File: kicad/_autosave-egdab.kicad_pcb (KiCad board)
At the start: 4 copper layers, 93.4 x 99.4 mm, 56 parts, among them J2 Conn_02x03_Counter_Clockwise, J3 Conn_02x04_Counter_Clockwise, SW1 SW_DIP_x04, SW2 SW_Push, SW6 SW_SPST, U1 ATtiny1606-S, U2 AS1115-BSST, U3 LM35-D

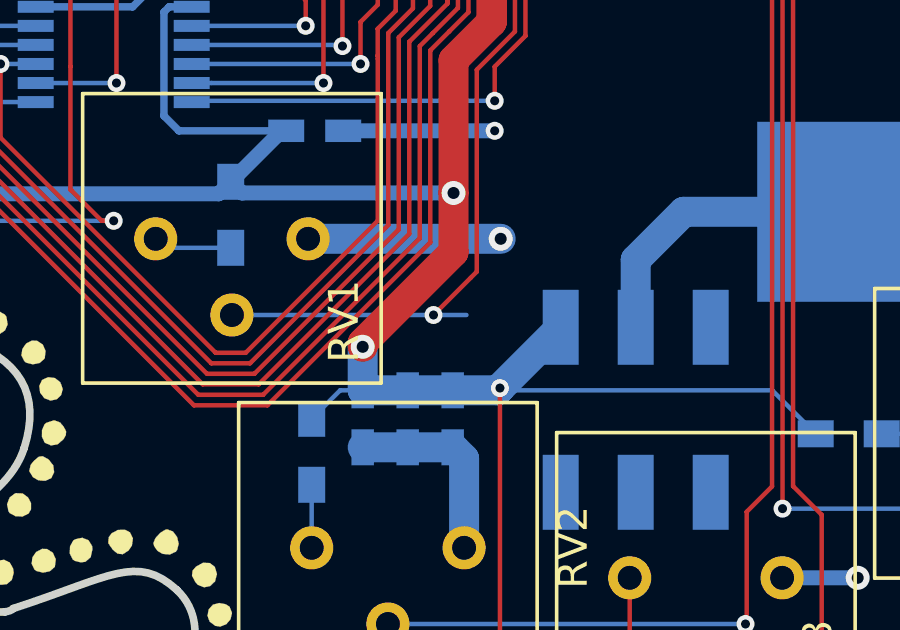
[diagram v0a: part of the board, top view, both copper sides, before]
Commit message: new board RGB LED controll and 7-seg digits
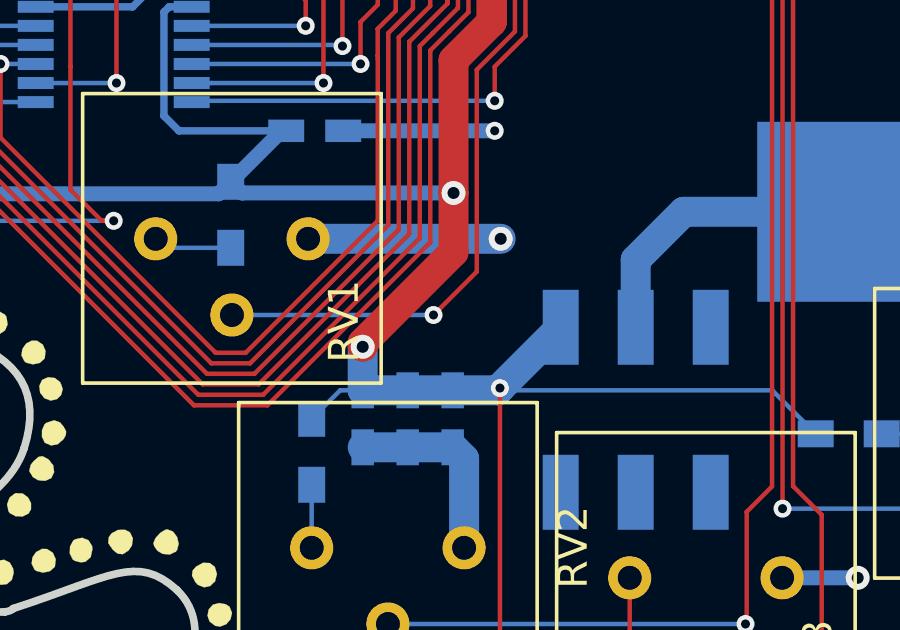
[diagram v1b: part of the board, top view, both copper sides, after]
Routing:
- net /P_LUMA: track 72.7 -> 71.6 mm
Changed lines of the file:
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@@
-(kicad_pcb (version 20171130) (host pcbnew "(5.1.2)-1")
+(kicad_pcb (version 20171130) (host pcbnew 5.1.5-1.fc30)
   (general
     (thickness 1.6)
     (drawings 203)
-    (tracks 1298)
+    (tracks 1297)
     (zones 0)
     (modules 56)
@@
     (34 B.Paste user hide)
     (35 F.Paste user)
-    (36 B.SilkS user hide)
-    (37 F.SilkS user)
+    (36 B.SilkS user)
+    (37 F.SilkS user hide)
     (38 B.Mask user hide)
-    (39 F.Mask user)
+    (39 F.Mask user hide)
     (40 Dwgs.User user hide)
     (41 Cmts.User user hide)
@@
     (45 Margin user hide)
     (46 B.CrtYd user hide)
-    (47 F.CrtYd user)
+    (47 F.CrtYd user hide)
     (48 B.Fab user hide)
-    (49 F.Fab user)
+    (49 F.Fab user hide)
   )
   (setup
-    (last_trace_width 0.25)
+    (last_trace_width 0.15)
     (user_trace_width 0.15)
     (user_trace_width 0.25)
@@
     (solder_mask_min_width 0.25)
     (aux_axis_origin 0 0)
-    (visible_elements 7FF7FFFF)
+    (visible_elements 7FFFFFFF)
     (pcbplotparams
       (layerselection 0x010f0_ffffffff)
@@
   (segment (start 216.6 77.1) (end 210.14 73.2) (width 0.15) (layer B.Cu) (net 44))
   (segment (start 170.34 129.14) (end 177.06 129.14) (width 0.15) (layer B.Cu) (net 45))
-  (segment (start 177.06 129.14) (end 178.16 129.14) (width 0.15) (layer B.Cu) (net 45))
   (via (at 177.06 129.14) (size 0.6) (drill 0.3) (layers F.Cu B.Cu) (net 45))
   (segment (start 177.06 129.14) (end 178.3 127.9) (width 0.15) (layer F.Cu) (net 45))
@@
   (segment (start 188.695 87.005) (end 188.695 87.005) (width 0.15) (layer B.Cu) (net 48))
   (via (at 188.695 87.005) (size 0.6) (drill 0.3) (layers F.Cu B.Cu) (net 48))
-  (segment (start 188.695 87.005) (end 188.695 135.595) (width 0.15) (layer F.Cu) (net 48))
   (segment (start 188.695 135.595) (end 188.695 135.595) (width 0.15) (layer F.Cu) (net 48))
   (via (at 188.695 135.595) (size 0.6) (drill 0.3) (layers F.Cu B.Cu) (net 48))
   (segment (start 196.695 135.595) (end 196.74 135.64) (width 0.15) (layer B.Cu) (net 48))
   (segment (start 188.695 135.595) (end 196.695 135.595) (width 0.15) (layer B.Cu) (net 48))
+  (segment (start 188.695 87.005) (end 188.695 135.595) (width 0.15) (layer F.Cu) (net 48))
   (segment (start 173 134.8) (end 173 136.9) (width 0.15) (layer B.Cu) (net 49))
   (segment (start 183.6 140.4) (end 183.5 140.5) (width 0.15) (layer B.Cu) (net 50))
